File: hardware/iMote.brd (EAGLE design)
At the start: 50 x 50 mm, 50 parts, among them CN1 USB-MINIB-UX60SC-MB, CN2 ICSP, CN3 PIN_Header, CN4 CC-HEADER, IC1 ATmega328P-AU, IC2 BLE112-A-VISUAL, IC3 FT232RLSSOP, Q2 BSS138, T1 2SD1718, Y1 16MHz

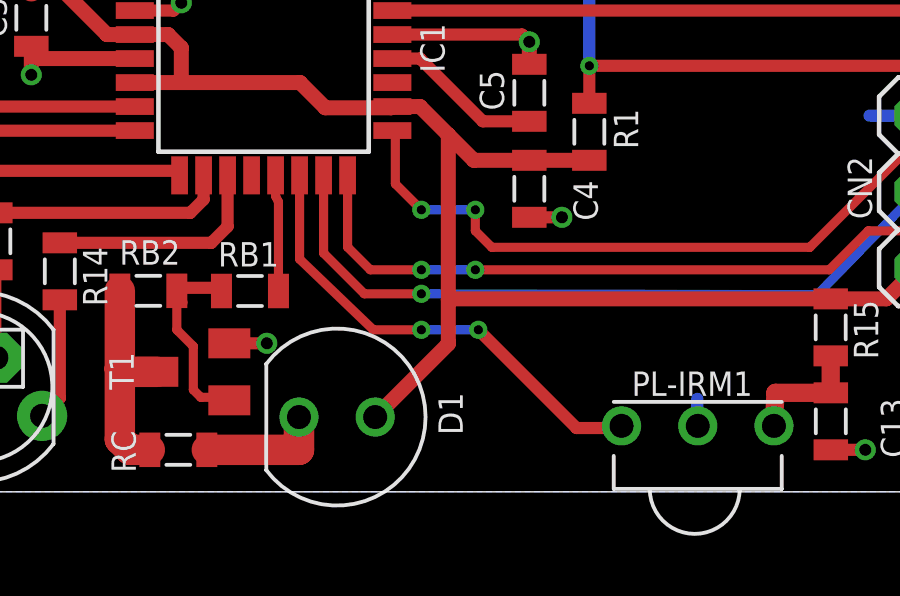
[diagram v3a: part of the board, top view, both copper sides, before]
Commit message: few fixes: * D2/BTN * D3/IROUT * D8/IRIN
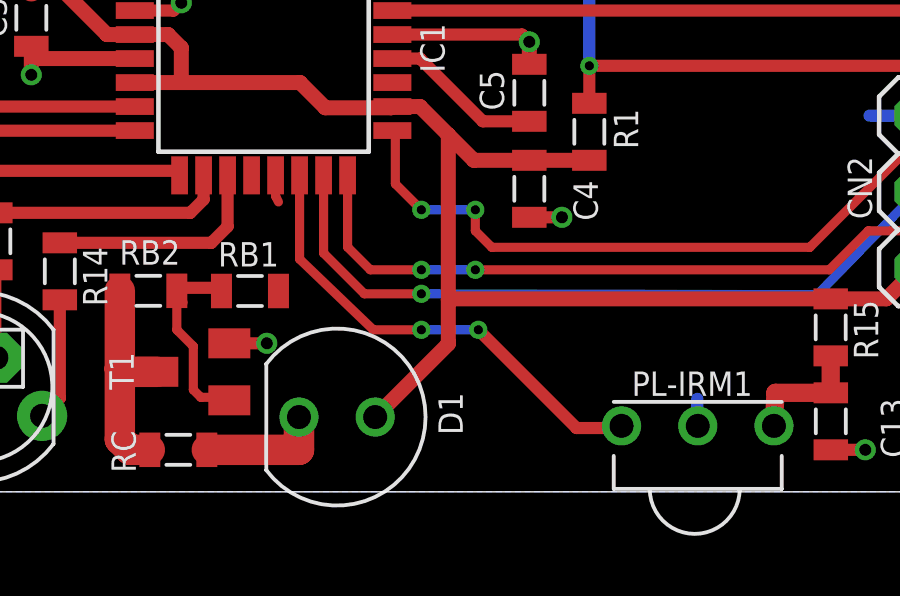
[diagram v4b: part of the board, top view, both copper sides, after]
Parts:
- D1: value OSIR5113A -> VSLB3940
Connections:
- removed net A2/BTN: R2.1, S1.2
- removed net D10/IRIN: IC1.14, PL-IRM1.1
- removed net D2_BTN: IC1.32
- removed net D9/IROUT: IC1.13, RB1.2
- new net D10: IC1.14
- new net D2/BTN: IC1.32, R2.1, S1.2
- new net D9: IC1.13
- net D3/IROUT: now also RB1.2
- net D8/IRIN: now also PL-IRM1.1
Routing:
- net D10/IRIN: track 15.9 -> 0.00 mm, vias 2 -> 0
- net D10: track 0.00 -> 15.8 mm, vias 0 -> 2
- net D2/BTN: track 0.00 -> 13.0 mm
- net A2/BTN: track 13.0 -> 0.00 mm
- net D9/IROUT: track 3.88 -> 0.00 mm
- net D9: track 0.00 -> 0.91 mm
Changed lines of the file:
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@@
 <attribute name="VALUE" x="43.732" y="4.72" size="1.27" layer="27" rot="R90"/>
 </element>
-<element name="D1" library="my" package="LED-3MM" value="OSIR5113A" x="24.992" y="2.492" smashed="yes" rot="R180">
+<element name="D1" library="my" package="LED-3MM" value="VSLB3940" x="24.992" y="2.492" smashed="yes" rot="R180">
 <attribute name="NAME" x="29.182" y="1.898" size="0.8128" layer="21" rot="R90"/>
 </element>
@@
 <signal name="D8/IRIN">
 <contactref element="IC1" pad="12"/>
+<contactref element="PL-IRM1" pad="1"/>
+<wire x1="22.142" y1="10.5494" x2="34.474" y2="2.198" width="0" layer="19" extent="1-1"/>
 </signal>
 <signal name="D3/IROUT">
 <contactref element="IC1" pad="1"/>
+<contactref element="RB1" pad="2"/>
+<wire x1="23.038" y1="6.694" x2="18.2494" y2="17.642" width="0" layer="19" extent="1-1"/>
 </signal>
 <signal name="RX_LV/BLERX">
@@
 <wire x1="11.3" y1="4.9274" x2="10.841" y2="4.4684" width="0.4064" layer="1"/>
 </signal>
-<signal name="D10/IRIN">
+<signal name="D10">
 <contactref element="IC1" pad="14"/>
-<contactref element="PL-IRM1" pad="1"/>
 <wire x1="23.742" y1="10.5494" x2="23.742" y2="7.758" width="0.3048" layer="1"/>
 <wire x1="23.742" y1="7.758" x2="26.2" y2="5.4" width="0.3048" layer="1"/>
@@
 <wire x1="27.8" y1="5.4" x2="29.7" y2="5.4" width="0.3048" layer="16"/>
 <via x="29.7" y="5.4" extent="1-16" drill="0.3048"/>
-<wire x1="34.474" y1="2.198" x2="34.474" y2="2.126" width="0.3048" layer="1"/>
 <wire x1="34.474" y1="2.126" x2="32.974" y2="2.126" width="0.4064" layer="1"/>
 <wire x1="32.974" y1="2.126" x2="29.7" y2="5.4" width="0.4064" layer="1"/>
 </signal>
-<signal name="D9/IROUT">
+<signal name="D9">
 <contactref element="IC1" pad="13"/>
-<contactref element="RB1" pad="2"/>
-<wire x1="23.038" y1="6.694" x2="23.038" y2="9.662" width="0.3048" layer="1"/>
 <wire x1="22.942" y1="10.5494" x2="22.942" y2="9.858" width="0.3048" layer="1"/>
 <wire x1="22.942" y1="9.858" x2="23.038" y2="9.662" width="0.3048" layer="1"/>
@@
 <wire x1="19.5914" y1="10.7" x2="19.742" y2="10.5494" width="0.4064" layer="1"/>
 </signal>
-<signal name="D2_BTN">
+<signal name="D2/BTN">
 <contactref element="IC1" pad="32"/>
-</signal>
-<signal name="A2/BTN">
 <contactref element="R2" pad="1"/>
 <wire x1="12.2" y1="14.85" x2="7.7" y2="14.85" width="0.6096" layer="1"/>
@@
 <wire x1="6.1804" y1="22.7269" x2="6.1804" y2="16.3696" width="0.6096" layer="1"/>
 <wire x1="6.1804" y1="16.3696" x2="7.7" y2="14.85" width="0.6096" layer="1"/>
+<wire x1="12.2" y1="14.85" x2="19.742" y2="19.1346" width="0" layer="19" extent="1-1"/>
 </signal>
 <signal name="A0">

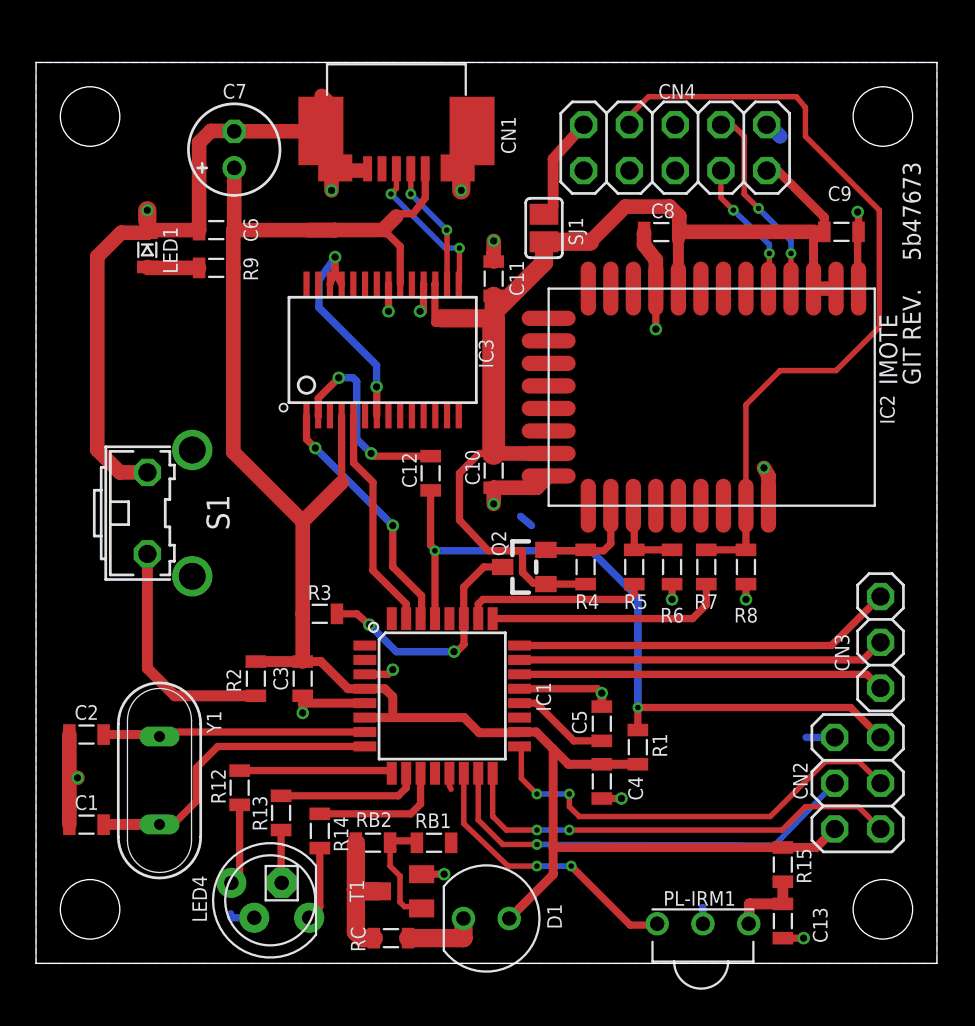
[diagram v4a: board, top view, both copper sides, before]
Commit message: IRIN:D10->D8, IROUT:D9->D3, TX_LV/BLETX<->RX_LV/BLERX
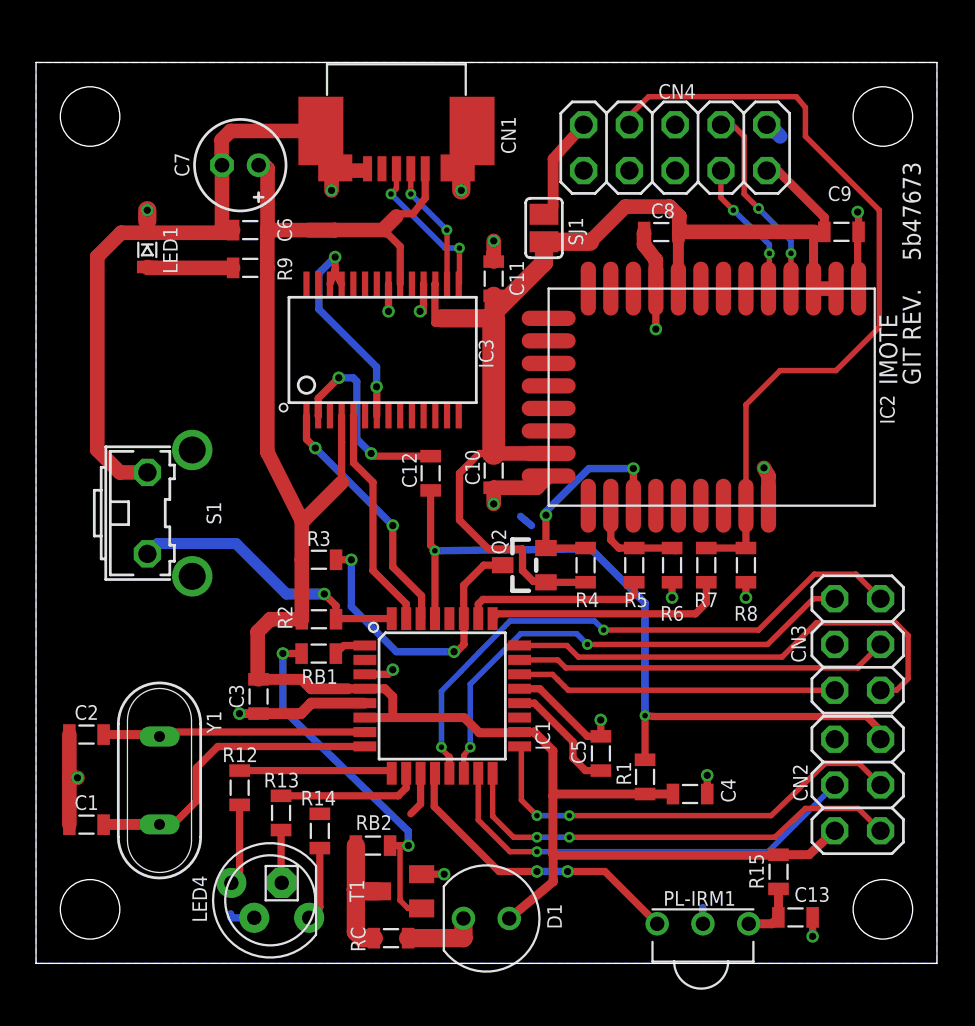
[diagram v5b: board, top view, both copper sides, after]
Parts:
- CN3: device my:PINHEAD-1X03 -> pinhead:2X03
- moved RB1 12.3 mm to (15.7, 17.2)
- moved C4 4.95 mm to (36.3, 9.40), turned to 180 degrees
- moved R2 4.81 mm to (15.7, 19.1), turned to 180 degrees
- moved R3 3.00 mm to (15.7, 22.4)
- moved C3 2.64 mm to (12.3, 14.8)
- moved C6 1.89 mm to (11.9, 40.7)
- moved R9 1.89 mm to (11.9, 38.6)
- moved R1 1.70 mm to (33.8, 10.3)
- moved C5 1.65 mm to (31.4, 11.7)
- moved CN3 1.28 mm to (45.6, 17.7), turned to 270 degrees
- moved C7 0.93 mm to (11.3, 44.3), turned to 180 degrees
- moved C13 0.73 mm to (42.1, 2.55), turned to 0 degrees
- moved R15 0.47 mm to (41.2, 5.08)
- moved RB2 0.16 mm to (18.7, 6.54)
- moved Q2 0.10 mm to (27.1, 22.1)
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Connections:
- new net N$14: IC1.2
- new net N$4: IC1.28
- new net N$6: IC1.19
- net A0: now also CN3.4; no longer CN3.2
- net A1: now also CN3.6; no longer CN3.3
- net A7: now also CN3.5; no longer CN3.1
- net D10: now also CN3.1
- net D9: now also CN3.2
- net GND: now also CN3.3
- net RX_LV/BLERX: now also IC2.P0_5; no longer IC2.P0_4
- net TX_LV/BLETX: now also IC2.P0_4; no longer IC2.P0_5
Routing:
- net D9: track 0.91 -> 32.8 mm, vias 0 -> 2
- net D8/IRIN: track 0.00 -> 17.0 mm, vias 0 -> 2
- net N$10: track 7.07 -> 20.1 mm, vias 0 -> 2
- net D10: track 15.8 -> 27.8 mm
- net A1: track 21.2 -> 27.1 mm
- net TX_LV/BLETX: track 6.27 -> 12.1 mm, vias 0 -> 2
- net D7/LED_B: track 7.52 -> 2.47 mm
- net D2/BTN: track 13.0 -> 16.0 mm, vias 0 -> 1
- net A4/RX_HV: track 13.9 -> 16.8 mm
- net A7: track 20.4 -> 17.9 mm
- net +5V: track 106.6 -> 108.7 mm
- net N$3: track 2.90 -> 4.78 mm
- net D3/IROUT: track 0.00 -> 1.80 mm
- net !RESET: track 41.4 -> 43.0 mm
- net AREF: track 5.43 -> 6.59 mm
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
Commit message: use less background straighter vcc shorter nets
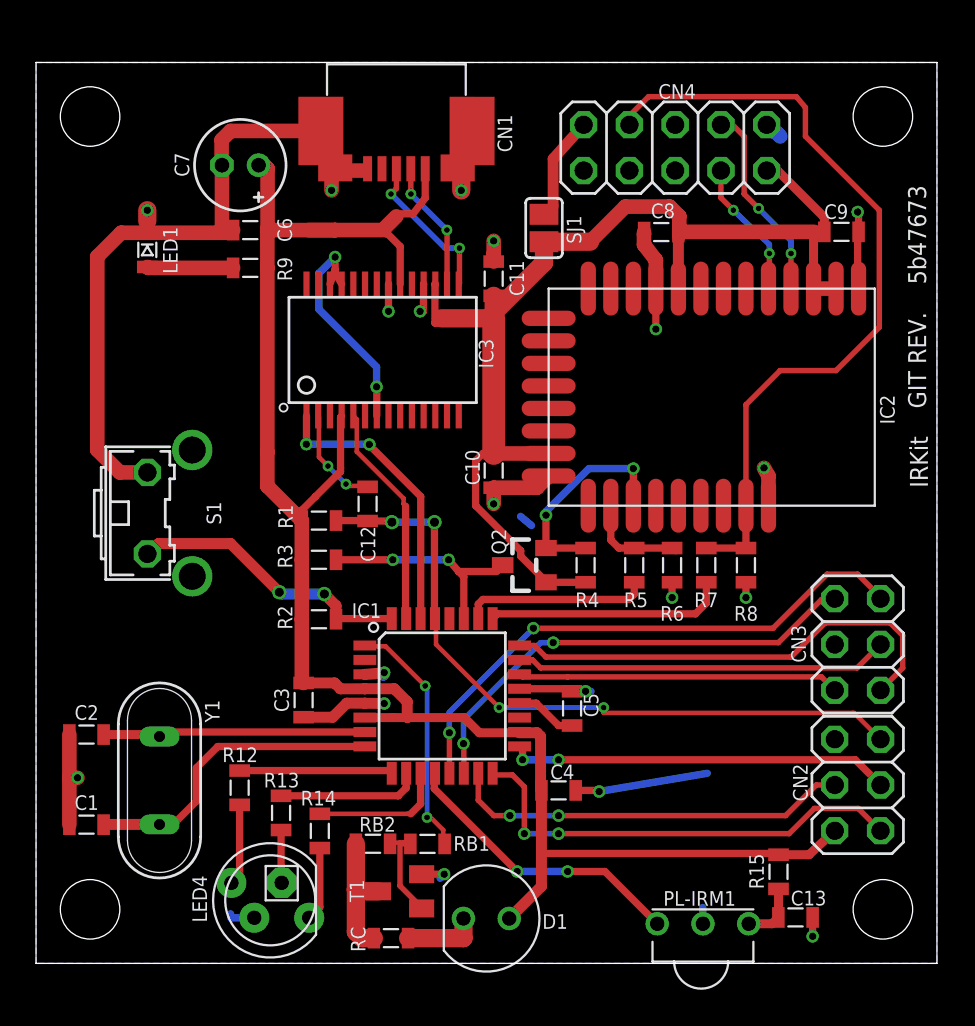
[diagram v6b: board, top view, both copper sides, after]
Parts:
- moved R1 23.0 mm to (15.7, 24.6), turned to 180 degrees
- moved RB1 12.2 mm to (21.7, 6.63)
- moved C4 7.30 mm to (29.0, 9.60)
- moved C12 3.89 mm to (18.4, 25.5)
- moved C5 2.97 mm to (29.8, 14.2)
- moved C3 2.51 mm to (14.8, 14.6)
- moved U$1 1.33 mm to (49.4, 30.8)
- moved RB2 0.10 mm to (18.7, 6.64)
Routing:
- net N$10: track 20.1 -> 5.43 mm, vias 2 -> 0
- net D3/IROUT: track 1.80 -> 13.8 mm, vias 0 -> 2
- net +5V: track 108.7 -> 98.7 mm
- net N$8: track 11.4 -> 5.77 mm
- net D7/LED_B: track 2.47 -> 7.52 mm
- net A4/RX_HV: track 16.8 -> 12.4 mm
- net D13/SCK: track 25.0 -> 21.3 mm
- net !RESET: track 43.0 -> 39.4 mm, vias 2 -> 4
- net AREF: track 6.59 -> 3.43 mm
- net +3V3: track 69.9 -> 66.9 mm
- net D11/MOSI: track 24.6 -> 22.3 mm, vias 1 -> 2
- net D0/USBRX: track 13.9 -> 15.9 mm
- net D9: track 32.8 -> 31.1 mm
- net GND: track 110.8 -> 112.1 mm
- net D10: track 27.8 -> 26.5 mm
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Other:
- board text added: "IRKit"
- board text removed: "IMOTE"
